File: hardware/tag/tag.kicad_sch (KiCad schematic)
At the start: 12 parts

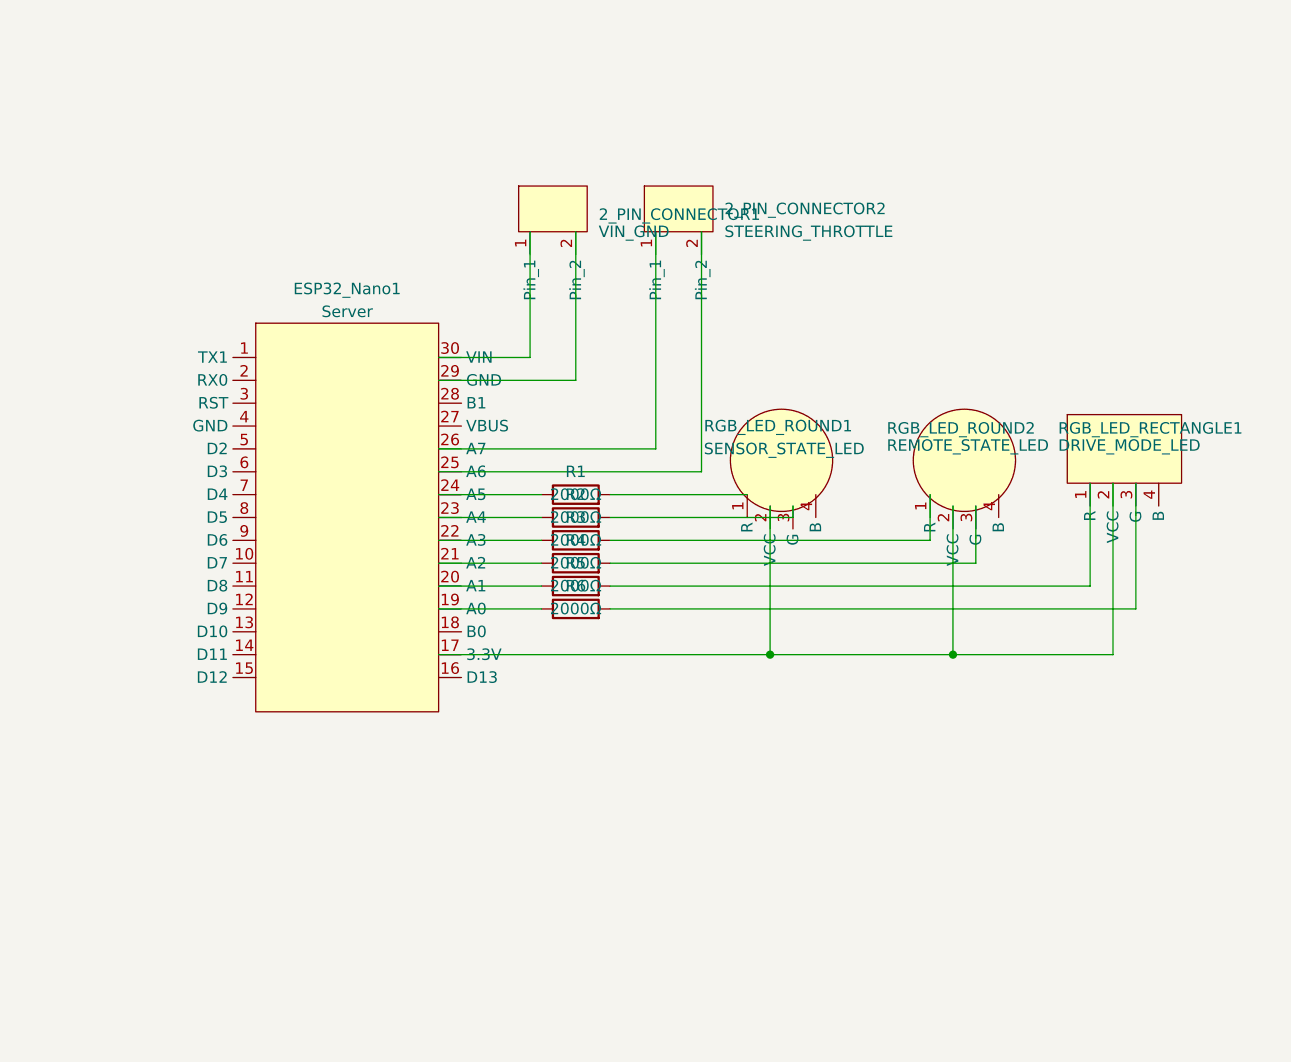
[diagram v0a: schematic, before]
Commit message: hardware/tag: Add Autocam Tag PCB.
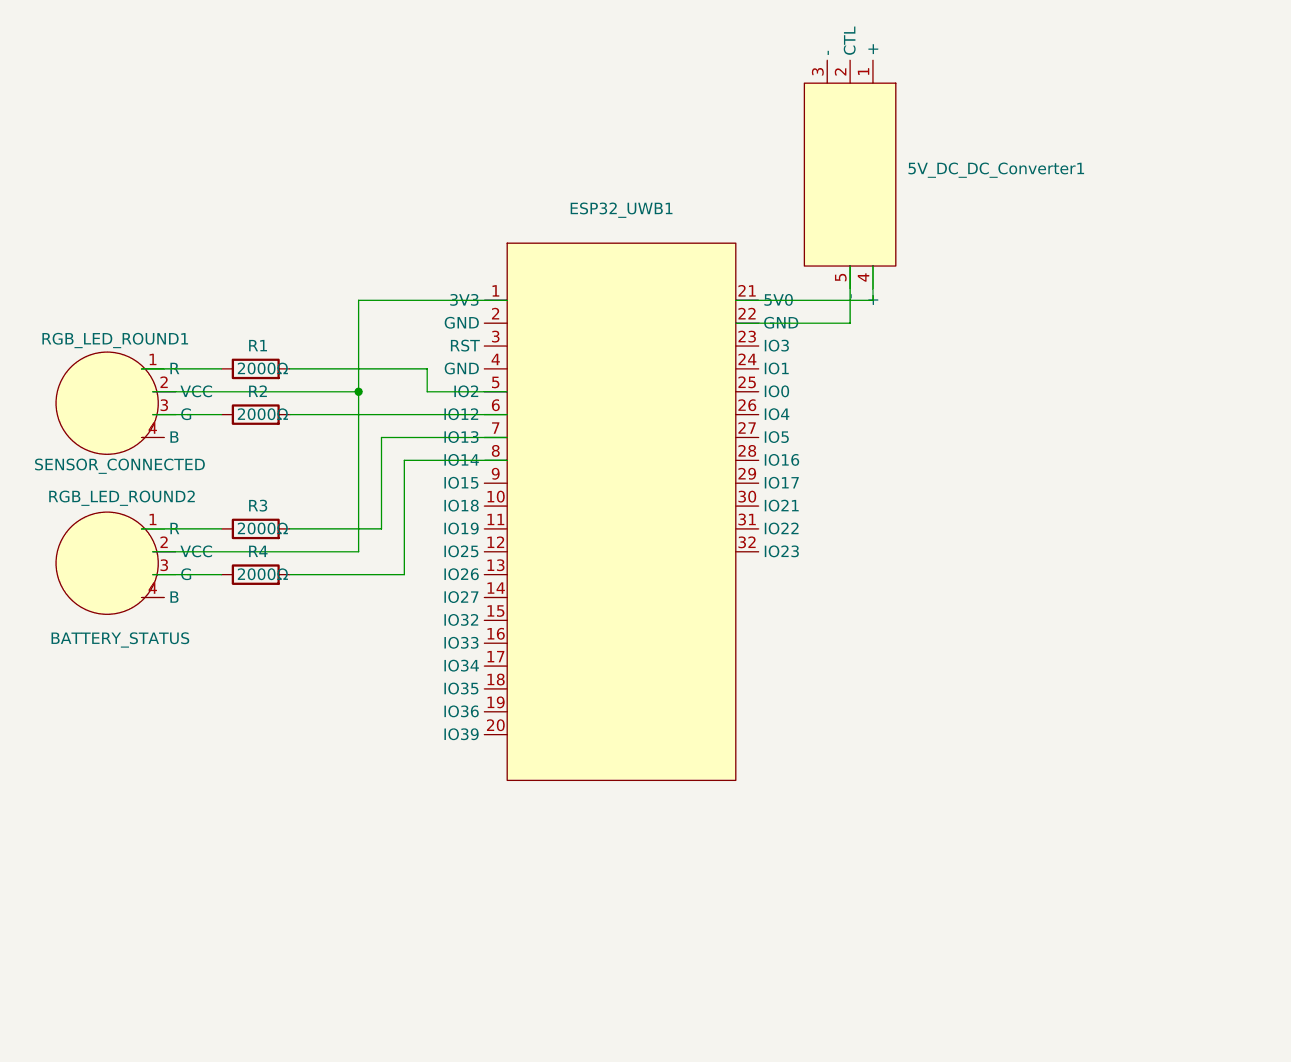
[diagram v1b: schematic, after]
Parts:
- removed 2_PIN_CONNECTOR1: VIN_GND, Autocam:2-PIN Connector, symbol Autocam:2_PIN_Connector
- removed 2_PIN_CONNECTOR2: STEERING_THROTTLE, Autocam:2-PIN Connector, symbol Autocam:2_PIN_Connector
- removed ESP32_Nano1: Server, Autocam:Arduino ESP32 Nano, symbol Autocam:Arduino_ESP32_Nano
- removed R5, R6: 2000Ω, Autocam:Simple Resistor, symbol Device:R
- removed RGB_LED_RECTANGLE1: DRIVE_MODE_LED, Autocam:Anode RGB LED (Rectangle), symbol Autocam:ANODE_RGB_LED_Rectangle
- added 5V_DC_DC_Converter1: ~, Autocam:5V DC-DC Step Up Converter (Rectangle), symbol Autocam:5V_DC_Converter_Rectangle
- added ESP32_UWB1: ~, Autocam:Makersfab ESP32 UWB, symbol Autocam:Makersfab_ESP32_UWB
- RGB_LED_ROUND1: value SENSOR_STATE_LED -> SENSOR_CONNECTED
- RGB_LED_ROUND2: value REMOTE_STATE_LED -> BATTERY_STATUS
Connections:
- net at R1.2: now also ESP32_UWB1.5 (IO2); no longer RGB_LED_ROUND1.1 (R)
- net at RGB_LED_ROUND1.2 (VCC), RGB_LED_ROUND2.2 (VCC): now also ESP32_UWB1.1 (3V3)
- net at R2.2: now also ESP32_UWB1.6 (IO12); no longer RGB_LED_ROUND1.3 (G)
- net at R2.1: now also RGB_LED_ROUND1.3 (G)
- net at R4.1: now also RGB_LED_ROUND2.3 (G)
- net at R4.2: now also ESP32_UWB1.8 (IO14); no longer RGB_LED_ROUND2.3 (G)
- net at R3.1: now also RGB_LED_ROUND2.1 (R)
- net at R1.1: now also RGB_LED_ROUND1.1 (R)
- net at R3.2: now also ESP32_UWB1.7 (IO13); no longer RGB_LED_ROUND2.1 (R)
- new net: 5V_DC_DC_Converter1.4 (+), ESP32_UWB1.21 (5V0)
- new net: 5V_DC_DC_Converter1.5 (-), ESP32_UWB1.22 (GND)
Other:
- title: Autocam Server -> Autocam Tag

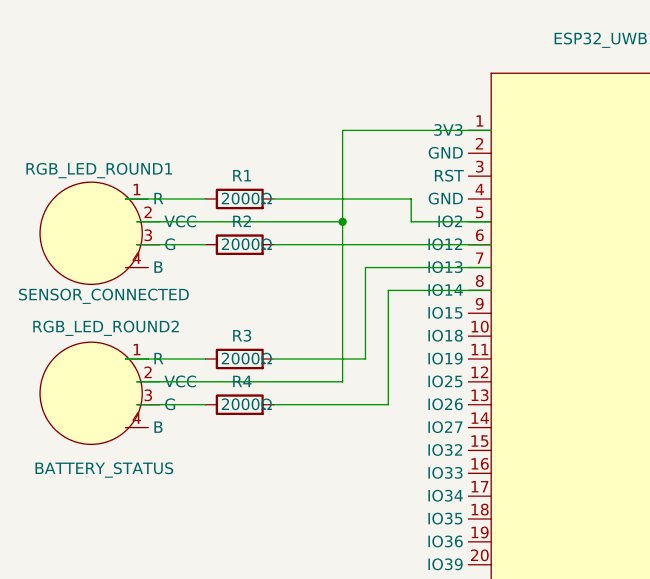
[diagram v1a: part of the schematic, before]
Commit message: hardware: Add more footprint measurement.
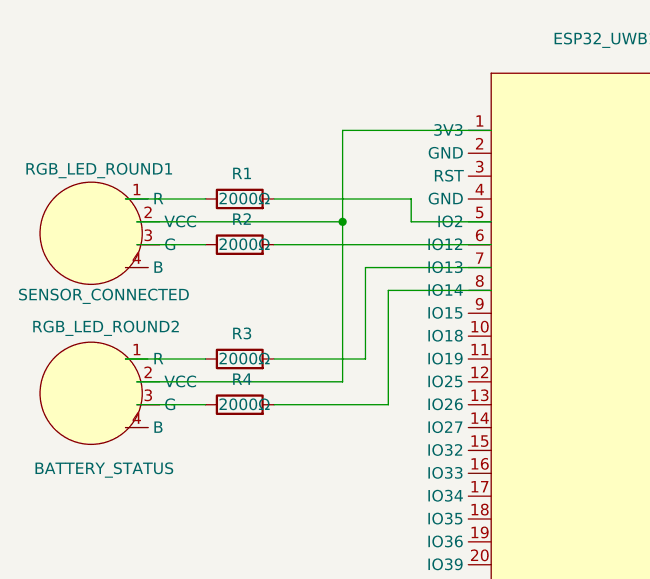
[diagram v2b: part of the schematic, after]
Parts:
- removed R1, R2, R3, R4: 2000Ω, Autocam:Simple Resistor, symbol Device:R
- added R1, R2, R3, R4: 2000Ω, Autocam:Simple Resistor, symbol Autocam:Simple Resistor
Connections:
- net at ESP32_UWB1.5 (IO2): now also R1.2
- net at ESP32_UWB1.6 (IO12): now also R2.2
- net at ESP32_UWB1.7 (IO13): now also R3.2
- net at ESP32_UWB1.8 (IO14): now also R4.2
- net at RGB_LED_ROUND2.1 (R): now also R3.1
- net at RGB_LED_ROUND2.3 (G): now also R4.1
- net at RGB_LED_ROUND1.1 (R): now also R1.1
- net at RGB_LED_ROUND1.3 (G): now also R2.1
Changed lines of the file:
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@@
+	)
+	(symbol
+		(lib_id "Autocam:Simple Resistor")
+		(at 107.95 110.49 90)
+		(unit 1)
+		(exclude_from_sim no)
+		(in_bom yes)
+		(on_board yes)
+		(dnp no)
+		(property "Reference" "R4"
+			(at 108.204 107.696 90)
+			(effects
+				(font
+					(size 1.27 1.27)
+				)
+			)
+		)
+		(property "Value" "2000Ω"
+			(at 108.458 110.49 90)
+			(effects
+				(font
+					(size 1.27 1.27)
+				)
+			)
+		)
+		(property "Footprint" "Autocam:Simple Resistor"
+			(at 107.95 112.268 90)
+			(effects
+				(font
+					(size 1.27 1.27)
+				)
+				(hide yes)
+			)
+		)
+		(property "Datasheet" "~"
+			(at 107.95 110.49 0)
+			(effects
+				(font
+					(size 1.27 1.27)
+				)
+				(hide yes)
+			)
+		)
+		(property "Description" "Resistor"
+			(at 107.95 110.49 0)
+			(effects
+				(font
+					(size 1.27 1.27)
+				)
+				(hide yes)
+			)
+		)
+		(pin "1"
+		)
+		(pin "2"
+		)
+		(instances
+			(project "tag"
+				(path "/3bb4c93b-765a-419c-8c17-50efa2d27859"
+					(reference "R4")
+					(unit 1)
+				)
+			)
+		)
+	)
+	(symbol
+		(lib_id "Autocam:Simple Resistor")
+		(at 107.95 105.41 90)
+		(unit 1)
+		(exclude_from_sim no)
+		(in_bom yes)
+		(on_board yes)
+		(dnp no)
+		(property "Reference" "R3"
+			(at 108.204 102.616 90)
+			(effects
+				(font
+					(size 1.27 1.27)
+				)
+			)
+		)
+		(property "Value" "2000Ω"
+			(at 108.458 105.41 90)
+			(effects
+				(font
+					(size 1.27 1.27)
+				)
+			)
+		)
+		(property "Footprint" "Autocam:Simple Resistor"
+			(at 107.95 107.188 90)
+			(effects
+				(font
+					(size 1.27 1.27)
+				)
+				(hide yes)
+			)
+		)
+		(property "Datasheet" "~"
+			(at 107.95 105.41 0)
+			(effects
+				(font
+					(size 1.27 1.27)
+				)
+				(hide yes)
+			)
+		)
+		(property "Description" "Resistor"
+			(at 107.95 105.41 0)
+			(effects
+				(font
+					(size 1.27 1.27)
+				)
+				(hide yes)
+			)
+		)
+		(pin "1"
+		)
+		(pin "2"
+		)
+		(instances
+			(project "tag"
+				(path "/3bb4c93b-765a-419c-8c17-50efa2d27859"
+					(reference "R3")
+					(unit 1)
+				)
+			)
+		)
 	)
 	(symbol
@@
 	)
 	(symbol
-		(lib_id "Device:R")
-		(at 107.95 105.41 90)
-		(unit 1)
-		(exclude_from_sim no)
-		(in_bom yes)
-		(on_board yes)
-		(dnp no)
-		(property "Reference" "R3"
-			(at 108.204 102.87 90)
-			(effects
-				(font
-					(size 1.27 1.27)
-				)
-			)
-		)
-		(property "Value" "2000Ω"
-			(at 108.712 105.41 90)
-			(effects
-				(font
-					(size 1.27 1.27)
-				)
-			)
-		)
-		(property "Footprint" "Autocam:Simple Resistor"
-			(at 107.95 107.188 90)
-			(effects
-				(font
-					(size 1.27 1.27)
-				)
-				(hide yes)
-			)
-		)
-		(property "Datasheet" "~"
-			(at 107.95 105.41 0)
-			(effects
-				(font
-					(size 1.27 1.27)
-				)
-				(hide yes)
-			)
-		)
-		(property "Description" "Resistor"
-			(at 107.95 105.41 0)
-			(effects
-				(font
-					(size 1.27 1.27)
-				)
-				(hide yes)
-			)
-		)
-		(pin "1"
-		)
-		(pin "2"
-		)
-		(instances
-			(project "tag"
-				(path "/3bb4c93b-765a-419c-8c17-50efa2d27859"
-					(reference "R3")
-					(unit 1)
-				)
-			)
-		)
-	)
-	(symbol
 		(lib_id "Autocam:ANODE_RGB_LED_Round")
 		(at 91.44 109.22 0)
@@
 	)
 	(symbol
+		(lib_id "Autocam:Simple Resistor")
+		(at 107.95 87.63 90)
+		(unit 1)
+		(exclude_from_sim no)
+		(in_bom yes)
+		(on_board yes)
+		(dnp no)
+		(property "Reference" "R1"
+			(at 108.204 84.836 90)
+			(effects
+				(font
+					(size 1.27 1.27)
+				)
+			)
+		)
+		(property "Value" "2000Ω"
+			(at 108.458 87.63 90)
+			(effects
+				(font
+					(size 1.27 1.27)
+				)
+			)
+		)
+		(property "Footprint" "Autocam:Simple Resistor"
+			(at 107.95 89.408 90)
+			(effects
+				(font
+					(size 1.27 1.27)
+				)
+				(hide yes)
+			)
+		)
+		(property "Datasheet" "~"
+			(at 107.95 87.63 0)
+			(effects
+				(font
+					(size 1.27 1.27)
+				)
+				(hide yes)
+			)
+		)
+		(property "Description" "Resistor"
+			(at 107.95 87.63 0)
+			(effects
+				(font
+					(size 1.27 1.27)
+				)
+				(hide yes)
+			)
+		)
+		(pin "1"
+		)
+		(pin "2"
+		)
+		(instances
+			(project ""
+				(path "/3bb4c93b-765a-419c-8c17-50efa2d27859"
+					(reference "R1")
+					(unit 1)
+				)
+			)
+		)
+	)
+	(symbol
 		(lib_id "Autocam:5V_DC_Converter_Rectangle")
 		(at 173.99 66.04 270)
@@
 	)
 	(symbol
-		(lib_id "Device:R")
-		(at 107.95 87.63 90)
-		(unit 1)
-		(exclude_from_sim no)
-		(in_bom yes)
-		(on_board yes)
-		(dnp no)
-		(property "Reference" "R1"
-			(at 108.204 85.09 90)
+		(lib_id "Autocam:Simple Resistor")
+		(at 107.95 92.71 90)
+		(unit 1)
+		(exclude_from_sim no)
+		(in_bom yes)
+		(on_board yes)
+		(dnp no)
+		(property "Reference" "R2"
+			(at 108.204 89.916 90)
 			(effects
 				(font
@@
 		)
 		(property "Value" "2000Ω"
-			(at 108.712 87.63 90)
-			(effects
-				(font
-					(size 1.27 1.27)
-				)
-			)
-		)
-		(property "Footprint" "Autocam:Simple Resistor"
-			(at 107.95 89.408 90)
-			(effects
-				(font
-					(size 1.27 1.27)
-				)
-				(hide yes)
-			)
-		)
-		(property "Datasheet" "~"
-			(at 107.95 87.63 0)
-			(effects
-				(font
-					(size 1.27 1.27)
-				)
-				(hide yes)
-			)
-		)
-		(property "Description" "Resistor"
-			(at 107.95 87.63 0)
-			(effects
-				(font
-					(size 1.27 1.27)
-				)
-				(hide yes)
-			)
-		)
-		(pin "1"
-		)
-		(pin "2"
-		)
-		(instances
-			(project ""
-				(path "/3bb4c93b-765a-419c-8c17-50efa2d27859"
-					(reference "R1")
-					(unit 1)
-				)
-			)
-		)
-	)
-	(symbol
-		(lib_id "Device:R")
-		(at 107.95 110.49 90)
-		(unit 1)
-		(exclude_from_sim no)
-		(in_bom yes)
-		(on_board yes)
-		(dnp no)
-		(property "Reference" "R4"
-			(at 108.204 107.95 90)
-			(effects
-				(font
-					(size 1.27 1.27)
-				)
-			)
-		)
-		(property "Value" "2000Ω"
-			(at 108.712 110.49 90)
-			(effects
-				(font
-					(size 1.27 1.27)
-				)
-			)
-		)
-		(property "Footprint" "Autocam:Simple Resistor"
-			(at 107.95 112.268 90)
-			(effects
-				(font
-					(size 1.27 1.27)
-				)
-				(hide yes)
-			)
-		)
-		(property "Datasheet" "~"
-			(at 107.95 110.49 0)
-			(effects
-				(font
-					(size 1.27 1.27)
-				)
-				(hide yes)
-			)
-		)
-		(property "Description" "Resistor"
-			(at 107.95 110.49 0)
-			(effects
-				(font
-					(size 1.27 1.27)
-				)
-				(hide yes)
-			)
-		)
-		(pin "1"
-		)
-		(pin "2"
-		)
-		(instances
-			(project "tag"
-				(path "/3bb4c93b-765a-419c-8c17-50efa2d27859"
-					(reference "R4")
-					(unit 1)
-				)
-			)
-		)
-	)
-	(symbol
-		(lib_id "Device:R")
-		(at 107.95 92.71 90)
-		(unit 1)
-		(exclude_from_sim no)
-		(in_bom yes)
-		(on_board yes)
-		(dnp no)
-		(property "Reference" "R2"
-			(at 108.204 90.17 90)
-			(effects
-				(font
-					(size 1.27 1.27)
-				)
-			)
-		)
-		(property "Value" "2000Ω"
-			(at 108.712 92.71 90)
-			(effects
-				(font
+			(at 108.458 92.71 90)
+			(effects
+				(font

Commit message: hardware: Add remote PCB.
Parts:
- added Battery_Charger1: ~, Autocam:USB-C 3.7V Lithium Battery Charger, symbol Autocam:USB-C_3.7V_Lithium_Battery_Charger
- added ON_OFF_SWITCH1: OFF ON, Autocam:3-PIN Switch, symbol Autocam:3_PIN_Switch
- added R5: 2000Ω, Autocam:Simple Resistor, symbol Autocam:Simple Resistor
- added RGB_LED_ROUND3: TAG_ACTIVE, Autocam:Anode RGB LED (Round), symbol Autocam:ANODE_RGB_LED_Round
- RGB_LED_ROUND1: value SENSOR_CONNECTED -> BATTERY
- RGB_LED_ROUND2: value BATTERY_STATUS -> SENSOR
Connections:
- net at ESP32_UWB1.1 (3V3), RGB_LED_ROUND1.2 (VCC), RGB_LED_ROUND2.2 (VCC): now also RGB_LED_ROUND3.2 (VCC)
- net at ESP32_UWB1.9 (IO15): now also R5.2
- net at 5V_DC_DC_Converter1.1 (+): now also Battery_Charger1.3 (OUT+)
- net at 5V_DC_DC_Converter1.3 (-): now also ON_OFF_SWITCH1.2
- new net: R5.1, RGB_LED_ROUND3.4 (B)
- new net: Battery_Charger1.6 (OUT-), ON_OFF_SWITCH1.3
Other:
- moved on the sheet: 5V_DC_DC_Converter1
